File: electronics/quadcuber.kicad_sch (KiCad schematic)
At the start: 0 parts

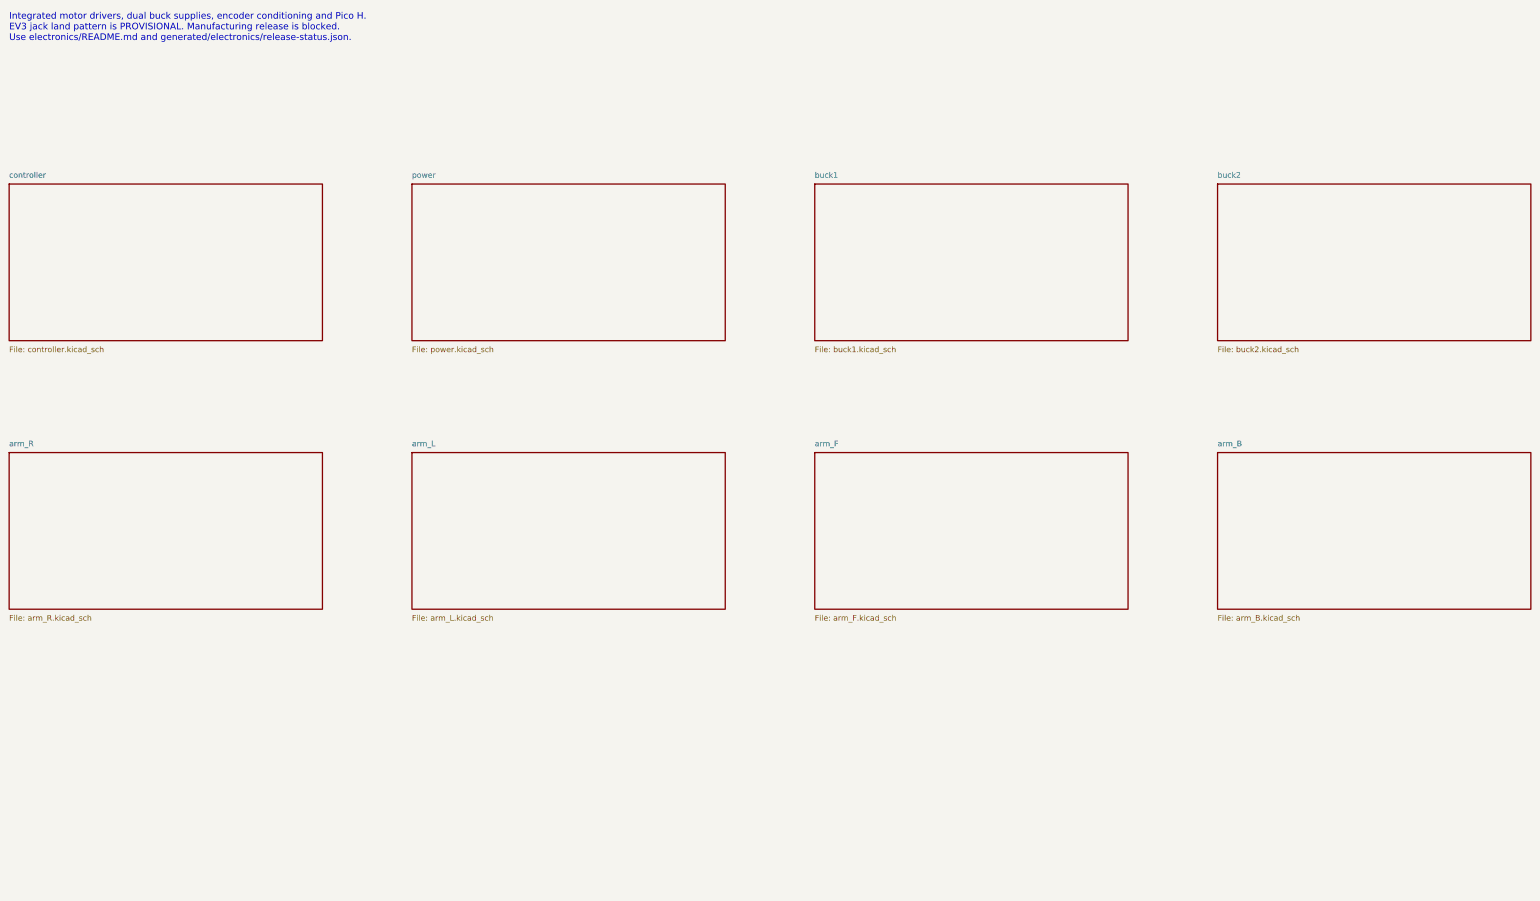
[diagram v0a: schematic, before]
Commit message: Integrate onboard RP2040 and drawing-based EV3 jacks on A1 PCB
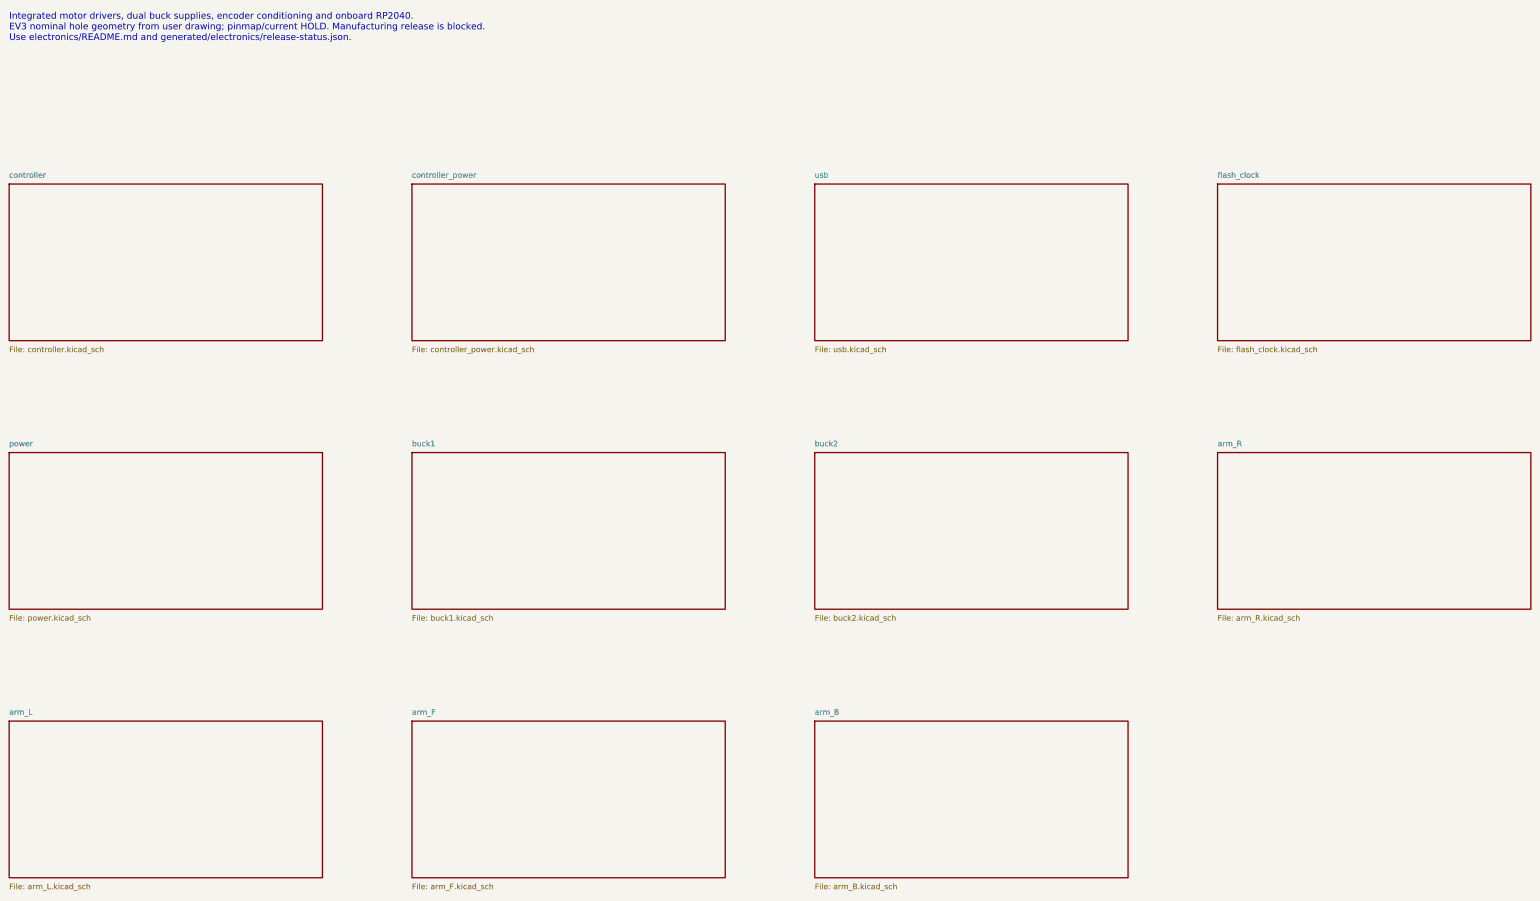
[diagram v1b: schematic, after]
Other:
- added sheet controller_power (controller_power.kicad_sch)
- added sheet flash_clock (flash_clock.kicad_sch)
- added sheet usb (usb.kicad_sch)
- note added: "Integrated motor drivers, dual buck supplies, encoder conditioning and onboard RP2040. EV3 nominal hole geometry from user drawing; pinmap/current HOLD. Manufacturing release is blocked. Use electronics/README.md and generated/electronics/release-status.json."
- note removed: "Integrated motor drivers, dual buck supplies, encoder conditioning and Pico H. EV3 jack land pattern is PROVISIONAL. Manufacturing release is blocked. Use electronics/README.md and generated/electronics/release-status.json."
- title: Quadcuber four-arm integrated controller - A0 ENGINEERING HOLD -> Quadcuber four-arm integrated controller - A1 ENGINEERING HOLD
